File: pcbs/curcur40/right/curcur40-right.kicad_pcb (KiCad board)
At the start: 2 copper layers, 124.3 x 91.8 mm, 81 parts

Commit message: fix error
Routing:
- net /KEY17: track 95.7 -> 87.0 mm
- net /KEY16: track 39.6 -> 39.0 mm
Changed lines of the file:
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@@
 		(fp_poly
 			(pts
-				(xy -4.05 -0.35) (xy -4.05 -1.5) (xy -2.8 -1.5)
+				(xy -4.05 -0.35) (xy -4.05 -1.5) (xy -3.8 -1.5)
 			)
 			(stroke
@@
 			(at 0 1.16 90)
 			(layer "B.SilkS")
+			(hide yes)
 			(effects
 				(font
@@
 		(fp_poly
 			(pts
-				(xy -4.05 -0.35) (xy -4.05 -1.5) (xy -2.8 -1.5)
+				(xy -4.05 -0.35) (xy -4.05 -1.5) (xy -3.8 -1.5)
 			)
 			(stroke
@@
 		(fp_poly
 			(pts
-				(xy -4.05 -0.35) (xy -4.05 -1.5) (xy -2.8 -1.5)
+				(xy -4.05 -0.35) (xy -4.05 -1.5) (xy -3.8 -1.5)
 			)
 			(stroke
@@
 		(fp_poly
 			(pts
-				(xy -4.05 -0.35) (xy -4.05 -1.5) (xy -2.8 -1.5)
+				(xy -4.05 -0.35) (xy -4.05 -1.5) (xy -3.8 -1.5)
 			)
 			(stroke
@@
 		(fp_poly
 			(pts
-				(xy -4.05 -0.35) (xy -4.05 -1.5) (xy -2.8 -1.5)
+				(xy -4.05 -0.35) (xy -4.05 -1.5) (xy -3.8 -1.5)
 			)
 			(stroke
@@
 			(at 1.01 1.925 90)
 			(layer "B.SilkS")
+			(hide yes)
 			(effects
 				(font
@@
 		(fp_poly
 			(pts
-				(xy -4.05 -0.35) (xy -4.05 -1.5) (xy -2.8 -1.5)
+				(xy -4.05 -0.35) (xy -4.05 -1.5) (xy -3.8 -1.5)
 			)
 			(stroke
@@
 		(fp_poly
 			(pts
-				(xy -4.05 -0.35) (xy -4.05 -1.5) (xy -2.8 -1.5)
+				(xy -4.05 -0.35) (xy -4.05 -1.5) (xy -3.8 -1.5)
 			)
 			(stroke
@@
 		(fp_poly
 			(pts
-				(xy -4.05 -0.35) (xy -4.05 -1.5) (xy -2.8 -1.5)
+				(xy -4.05 -0.35) (xy -4.05 -1.5) (xy -3.8 -1.5)
 			)
 			(stroke
@@
 		(fp_poly
 			(pts
-				(xy -4.05 -0.35) (xy -4.05 -1.5) (xy -2.8 -1.5)
+				(xy -4.05 -0.35) (xy -4.05 -1.5) (xy -3.8 -1.5)
 			)
 			(stroke
@@
 		(fp_poly
 			(pts
-				(xy -4.05 -0.35) (xy -4.05 -1.5) (xy -2.8 -1.5)
+				(xy -4.05 -0.35) (xy -4.05 -1.5) (xy -3.8 -1.5)
 			)
 			(stroke
@@
 		(fp_poly
 			(pts
-				(xy -4.05 -0.35) (xy -4.05 -1.5) (xy -2.8 -1.5)
+				(xy -4.05 -0.35) (xy -4.05 -1.5) (xy -3.8 -1.5)
 			)
 			(stroke
@@
 			(at -0.06875 -1.114992 90)
 			(layer "B.SilkS")
+			(hide yes)
 			(effects
 				(font
@@
 			(at 1.02725 2.005 90)
 			(layer "B.SilkS")
+			(hide yes)
 			(effects
 				(font
@@
 		(fp_poly
 			(pts
-				(xy -4.05 -0.35) (xy -4.05 -1.5) (xy -2.8 -1.5)
+				(xy -4.05 -0.35) (xy -4.05 -1.5) (xy -3.8 -1.5)
 			)
 			(stroke
@@
 		(fp_poly
 			(pts
-				(xy -4.05 -0.35) (xy -4.05 -1.5) (xy -2.8 -1.5)
+				(xy -4.05 -0.35) (xy -4.05 -1.5) (xy -3.8 -1.5)
 			)
 			(stroke
@@
 		(fp_poly
 			(pts
-				(xy -4.05 -0.35) (xy -4.05 -1.5) (xy -2.8 -1.5)
+				(xy -4.05 -0.35) (xy -4.05 -1.5) (xy -3.8 -1.5)
 			)
 			(stroke
@@
 		(fp_poly
 			(pts
-				(xy -4.05 -0.35) (xy -4.05 -1.5) (xy -2.8 -1.5)
+				(xy -4.05 -0.35) (xy -4.05 -1.5) (xy -3.8 -1.5)
 			)
 			(stroke
@@
 		(fp_poly
 			(pts
-				(xy -4.05 -0.35) (xy -4.05 -1.5) (xy -2.8 -1.5)
+				(xy -4.05 -0.35) (xy -4.05 -1.5) (xy -3.8 -1.5)
 			)
 			(stroke
@@
 		(fp_poly
 			(pts
-				(xy -4.05 -0.35) (xy -4.05 -1.5) (xy -2.8 -1.5)
+				(xy -4.05 -0.35) (xy -4.05 -1.5) (xy -3.8 -1.5)
 			)
 			(stroke
@@
 		(fp_poly
 			(pts
-				(xy -4.05 -0.35) (xy -4.05 -1.5) (xy -2.8 -1.5)
+				(xy -4.05 -0.35) (xy -4.05 -1.5) (xy -3.8 -1.5)
 			)
 			(stroke
@@
 		(fp_poly
 			(pts
-				(xy -4.05 -0.35) (xy -4.05 -1.5) (xy -2.8 -1.5)
+				(xy -4.05 -0.35) (xy -4.05 -1.5) (xy -3.8 -1.5)
 			)
 			(stroke
@@
 	)
 	(segment
+		(start 96.8 37.25)
+		(end 98.05 36)
+		(width 0.2032)
+		(layer "B.Cu")
+		(net "/KEY17")
+	)
+	(segment
 		(start 80.15 43.22)
 		(end 80.15 40.604)
@@
 	)
 	(segment
-		(start 99.0071 35.857718)
-		(end 99.0071 18.03665)
+		(start 98.05 36)
+		(end 99.01 36)
 		(width 0.2032)
 		(layer "B.Cu")
@@
 	)
 	(segment
-		(start 87.33 40.05)
-		(end 89.5 36.2)
-		(width 0.25)
+		(start 99.0071 35.857718)
+		(end 99.0071 18.03665)
+		(width 0.2032)
 		(layer "B.Cu")
 		(net "/KEY17")
 	)
 	(segment
-		(start 87.327906 40.05405)
-		(end 90.015704 37.36625)
+		(start 87.328 40.054)
+		(end 90.132 37.25)
 		(width 0.2032)
 		(layer "B.Cu")
@@
 	)
 	(segment
-		(start 99.0071 18.03665)
-		(end 101.4375 15.60625)
+		(start 99.01 36)
+		(end 99.01 35.86)
 		(width 0.2032)
 		(layer "B.Cu")
@@
 	)
 	(segment
-		(start 96.5 36.2)
-		(end 99.01 35.86)
-		(width 0.25)
+		(start 99.0071 18.03665)
+		(end 101.4375 15.60625)
+		(width 0.2032)
 		(layer "B.Cu")
 		(net "/KEY17")
 	)
 	(segment
-		(start 89.5 36.2)
-		(end 96.5 36.2)
-		(width 0.25)
+		(start 90.132 37.25)
+		(end 96.8 37.25)
+		(width 0.2032)
 		(layer "B.Cu")
 		(net "/KEY17")
@@
 	)
 	(segment
-		(start 87.33 40.05)
-		(end 89.5 36.2)
-		(width 0.25)
-		(layer "B.Cu")
-		(net "/KEY17")
-	)
-	(segment
 		(start 81.803802 0.15125)
 		(end 87.2175 0.15125)
@@
 	)
 	(segment
+		(start 6.543 38.546)
+		(end 7.6 38.546)
+		(width 0.4)
+		(layer "B.Cu")
+		(net "+5VR")
+	)
+	(segment
 		(start 20.972508 -15.95)
 		(end 20.972508 -15.43125)
@@
 	)
 	(segment
+		(start 17.402 38.146)
+		(end 18.598 38.696)
+		(width 0.4)
+		(layer "B.Cu")
+		(net "+5VR")
+	)
+	(segment
 		(start 46.132502 35.076252)
 		(end 46.2125 35.15625)
@@
 	)
 	(segment
-		(start 26.3875 2.92625)
-		(end 26.4475 2.86625)
-		(width 0.508)
+		(start 7.6 38.546)
+		(end 8 38.146)
+		(width 0.4)
 		(layer "B.Cu")
 		(net "+5VR")
 	)
 	(segment
-		(start 6.5425 38.54625)
-		(end 6.6925 38.6962)
+		(start 8 38.146)
+		(end 17.402 38.146)
 		(width 0.4)
 		(layer "B.Cu")
@@
 	)
 	(segment
-		(start 6.6925 38.6962)
-		(end 18.5975 38.6962)
-		(width 0.4)
+		(start 26.3875 2.92625)
+		(end 26.4475 2.86625)
+		(width 0.508)
 		(layer "B.Cu")
 		(net "+5VR")
@@
 	)
 	(segment
+		(start 95.8 36.573)
+		(end 96.859 35.514)
+		(width 0.2032)
+		(layer "B.Cu")
+		(net "/KEY18")
+	)
+	(segment
 		(start 100.3875 -3.44375)
 		(end 101.4375 -3.44375)
@@
 	)
 	(segment
-		(start 87.002168 39.26765)
-		(end 89.696767 36.57305)
+		(start 98.2207 35.514118)
+		(end 98.2207 -1.27695)
 		(width 0.2032)
 		(layer "B.Cu")
@@
 	)
 	(segment
-		(start 89.696767 36.57305)
-		(end 97.161768 36.57305)
+		(start 87.002 39.268)
+		(end 89.697 36.573)
 		(width 0.2032)
 		(layer "B.Cu")
@@
 	)
 	(segment
-		(start 98.2207 35.514118)
-		(end 98.2207 -1.27695)
+		(start 89.697 36.573)
+		(end 95.8 36.573)
 		(width 0.2032)
 		(layer "B.Cu")
@@
 	)
 	(segment
-		(start 97.161768 36.57305)
-		(end 98.2207 35.514118)
+		(start 96.859 35.514)
+		(end 98.221 35.514)
 		(width 0.2032)
 		(layer "B.Cu")
@@
 	)
 	(segment
-		(start 88.7375 39.866169)
-		(end 90.380119 38.22355)
+		(start 96 37.85)
+		(end 96.7 40.1)
 		(width 0.2032)
 		(layer "B.Cu")
@@
 	)
 	(segment
-		(start 90 39.75)
-		(end 99.8 39.75)
-		(width 0.25)
-		(layer "B.Cu")
-		(net "/KEY16")
-	)
-	(segment
 		(start 71.17 40.23995)
 		(end 71.17 40.74265)
@@
 	)
 	(segment
-		(start 99.8 39.75)
-		(end 101.32 34.66)
-		(width 0.25)
+		(start 88.737 40.426)
+		(end 90.1 37.85)
+		(width 0.2032)
 		(layer "B.Cu")
 		(net "/KEY16")
 	)
 	(segment
-		(start 88.74 39.87)
-		(end 90 39.75)
-		(width 0.25)
+		(start 99.8 40.1)
+		(end 101.32 34.66)
+		(width 0.2032)
 		(layer "B.Cu")
 		(net "/KEY16")
 	)
 	(segment
-		(start 88.7375 40.42625)
-		(end 88.7375 39.866169)
+		(start 96.7 40.1)
+		(end 99.8 40.1)
 		(width 0.2032)
 		(layer "B.Cu")
@@
 	)
 	(segment
-		(start 88.74 39.87)
-		(end 90 39.75)
-		(width 0.25)
+		(start 71.17 40.74265)
+		(end 71.1175 40.79515)
+		(width 0.2032)
 		(layer "B.Cu")
 		(net "/KEY16")
 	)
 	(segment
-		(start 71.17 40.74265)
-		(end 71.1175 40.79515)
+		(start 90.1 37.85)
+		(end 96 37.85)
 		(width 0.2032)
 		(layer "B.Cu")

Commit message: fix led
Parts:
- moved rLED8 1.31 mm to (52.4, 47.6)
- moved rLED1 1.06 mm to (33.3, 47.6)
- moved rLED9 1.06 mm to (71.4, 47.6)
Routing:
- net GNDR: track 147.1 -> 175.5 mm
- net Net-(rD1-K): track 473.8 -> 469.5 mm
- net Net-(rLED7-DOUT): track 48.6 -> 45.4 mm
- net Net-(rLED8-DOUT): track 47.9 -> 50.3 mm
- net Net-(rLED10-DIN): track 69.6 -> 70.7 mm
- net /LED: track 51.2 -> 50.2 mm

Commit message: fix
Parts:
- rU4: footprint Package_SO:SOIC-8_5.23x5.23mm_P1.27mm -> Package_SO:SOIC-8_5.3x5.3mm_P1.27mm
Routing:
- net /NCS: track 170.5 -> 153.6 mm
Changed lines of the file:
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@@
 		)
 	)
-	(footprint "Package_SO:SOIC-8_5.23x5.23mm_P1.27mm"
+	(footprint "Package_SO:SOIC-8_5.3x5.3mm_P1.27mm"
 		(layer "B.Cu")
 		(at 63.1375 13.78625 180)
@@
 		(layer "F.Cu")
 		(net "/NCS")
-	)
-	(segment
-		(start 0.5 39.8)
-		(end 0.5 56.691)
-		(width 0.2)
-		(layer "F.Cu")
-		(net "/NCS")

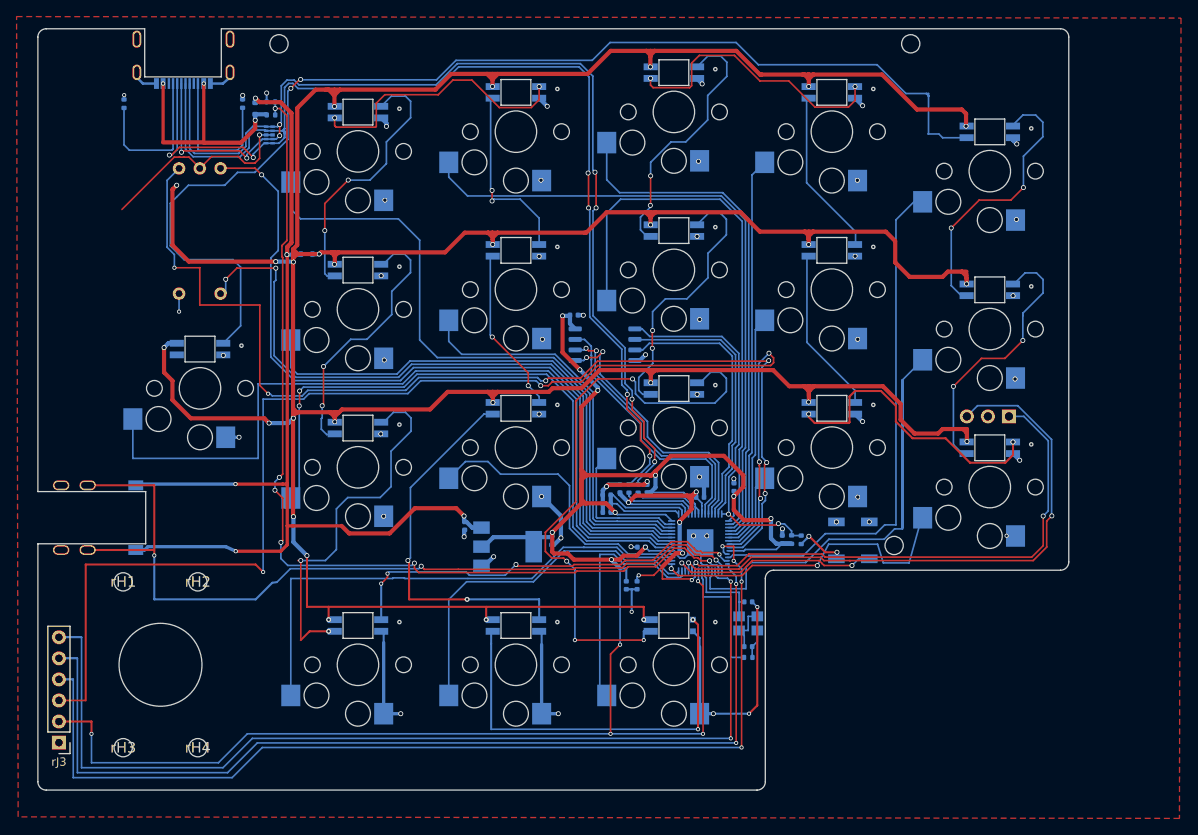
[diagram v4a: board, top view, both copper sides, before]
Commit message: 🔴 1. 致命的な不具合（Critical：物理的に組立不可、または動作不可）
[Critical-1] トラックボール部の3D機構・光学設計の破綻（4重の物理的干渉・焦点外れ）
[Critical-2] 左右メイン基板の取付穴径が ∅2.20 mm になっており、M2スペーサーが貫通できない
[Critical-3] 3Dプリントケース内部の 2.0mm スペーサー受けボスが消失しており、高さが 2.0 mm 合わない
[Critical-4] PMW3360 センサー基板のプルアップ抵抗 R1（10kΩ）が PCBA の BOM/CPL から除外されており、リセット端子（NRESET）がフローティング（不定）になる
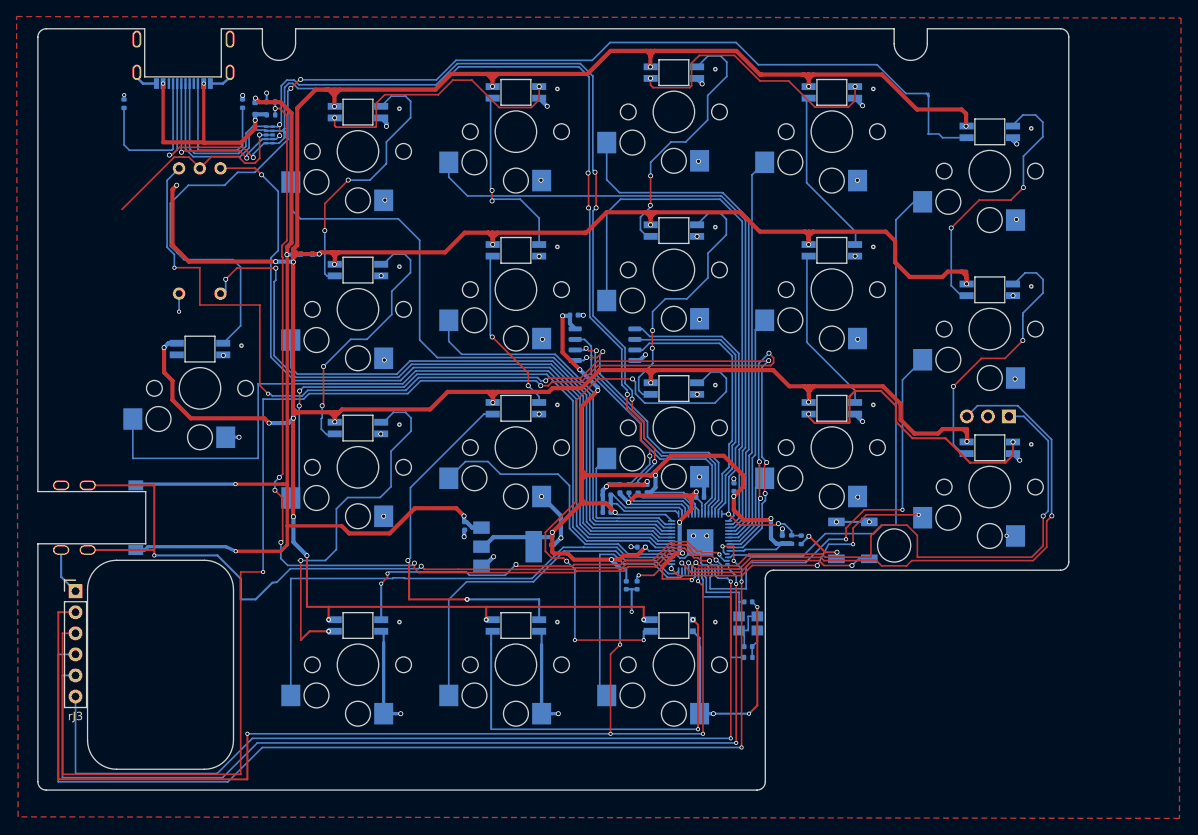
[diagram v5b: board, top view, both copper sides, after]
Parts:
- removed rH1, rH2, rH3, rH4: MountingHole_2.2mm_M2, 
- moved rJ3 18.4 mm to (-0.72, 43.5), turned to 0 degrees
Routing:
- net /KEY17: track 87.0 -> 50.8 mm, vias 0 -> 2
- net /NCS: track 153.6 -> 179.4 mm
- net +3V3R: track 287.1 -> 308.5 mm
- net /SCLK: track 122.6 -> 111.7 mm
- net GNDR: track 175.5 -> 185.2 mm
- net /SWCLK: track 63.4 -> 69.7 mm
- net /MISO: track 124.7 -> 128.9 mm
- net /KEY16: track 39.0 -> 36.0 mm, vias 2 -> 4
- net /MOSI: track 121.3 -> 119.0 mm
- net /TX: track 103.0 -> 101.3 mm
- net /SWD: track 71.6 -> 72.1 mm
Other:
- outline, holes or cut-outs redrawn

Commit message: mv trackball hole
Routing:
- net GNDR: track 185.2 -> 244.0 mm
- net /MOSI: track 119.0 -> 123.7 mm
- net /MISO: track 128.9 -> 133.5 mm
- net +3V3R: track 308.5 -> 311.0 mm
- net /SCLK: track 111.7 -> 112.8 mm
- net /NCS: track 179.4 -> 180.5 mm
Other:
- outline, holes or cut-outs redrawn
